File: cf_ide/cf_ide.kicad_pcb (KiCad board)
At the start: 2 copper layers, 17 parts, among them J1 PATA_44pin, J2 Compact_Flash_TrueIDE, U1 74AHC1G02, U2 LT1761-3.3

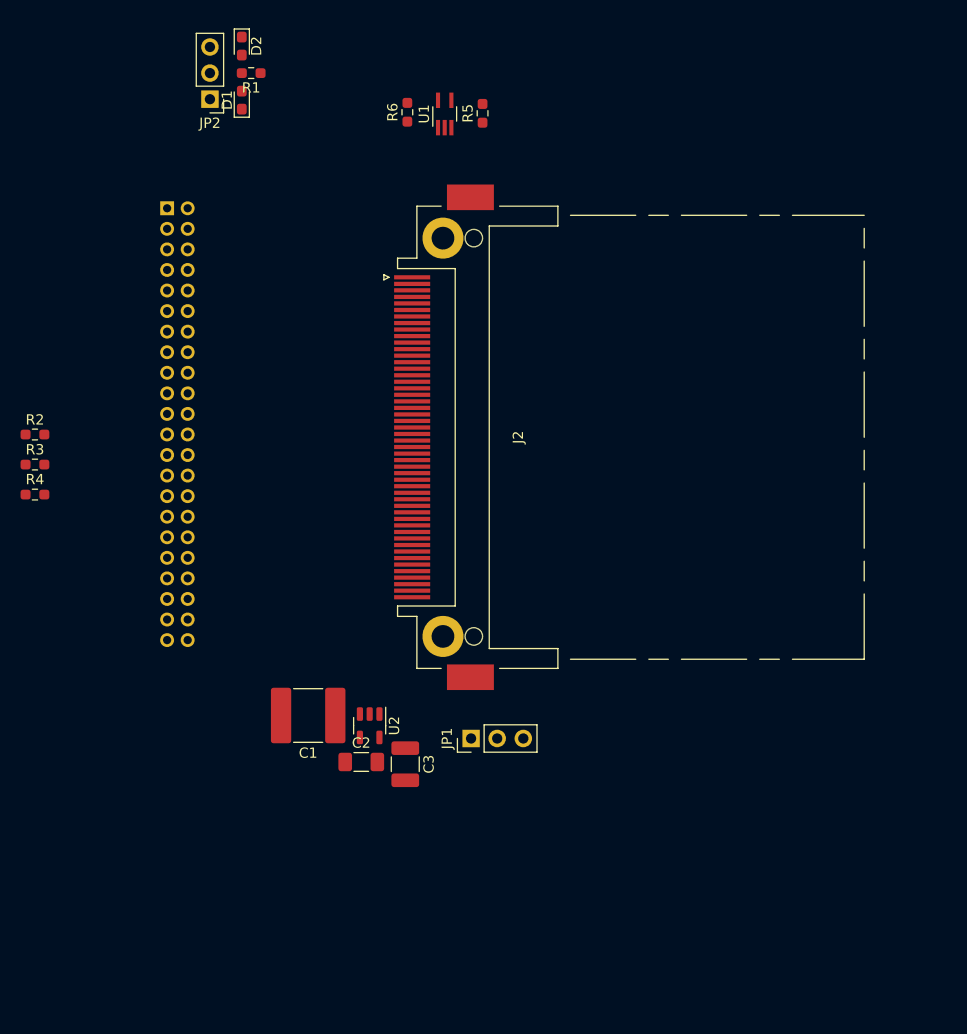
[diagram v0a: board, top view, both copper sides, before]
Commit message: Remove unneeded pull up/downs
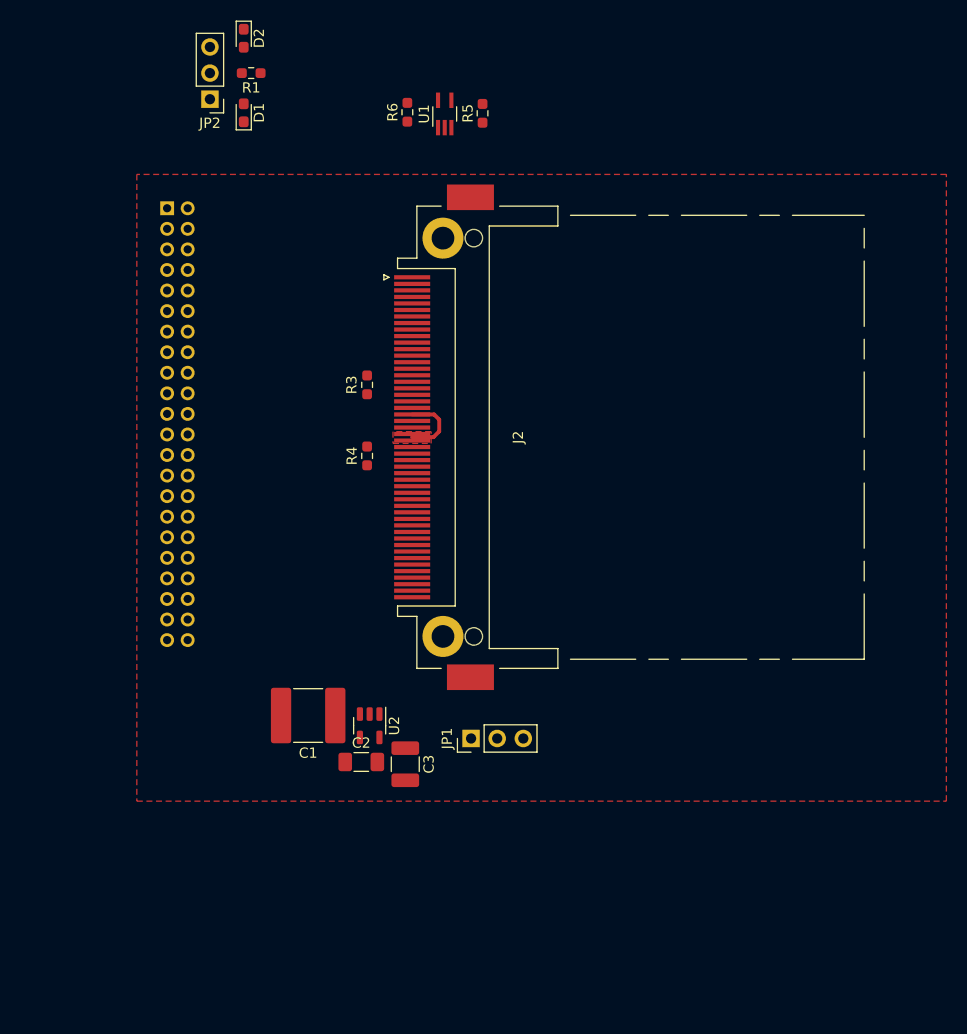
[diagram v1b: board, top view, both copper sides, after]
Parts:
- removed R2: R, Resistor_SMD:R_0603_1608Metric_Pad0.98x0.95mm_HandSolder
- R3, R4: value R -> 47k
- moved R3 33.2 mm to (124.0, 91.6), turned to -90 degrees
- moved R4 32.5 mm to (124.0, 98.5), turned to 90 degrees
- moved D1 1.24 mm to (112.0, 65.1)
- moved D2 0.78 mm to (112.0, 57.9)
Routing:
- net VCC: track 0.00 -> 6.86 mm
- added copper zone on F.Cu, net GNDD
- added copper zone on F.Cu, net VCC

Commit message: Start PCB design
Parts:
- C1: footprint Capacitor_SMD:C_2220_5650Metric_Pad1.97x5.40mm_HandSolder -> Capacitor_SMD:C_0805_2012Metric_Pad1.18x1.45mm_HandSolder; moved to B.Cu
- C2: value 0.1μF -> 0.01μF; moved to B.Cu
- C3, JP1, R3, R4, U2: moved to B.Cu
- moved D1 85.7 mm to (116.8, 150.7)
- moved D2 85.7 mm to (116.8, 143.4)
- moved JP2 85.7 mm to (113.5, 149.4)
- moved R1 85.7 mm to (117.5, 146.8)
- moved R5 75.7 mm to (134.9, 140.8)
- moved R6 75.7 mm to (127.6, 140.7)
- moved U1 75.7 mm to (131.2, 140.9)
- moved C2 64.7 mm to (120.8, 63.7), turned to -90 degrees
- moved C3 61.2 mm to (119.5, 67.8), turned to 180 degrees
- moved U2 60.9 mm to (117.3, 64.2), turned to 0 degrees
- moved C1 56.7 mm to (114.8, 67.2)
- moved JP1 56.1 mm to (124.0, 70.9), turned to 0 degrees
- moved R4 8.59 mm to (132.6, 98.7)
- moved R3 8.59 mm to (132.6, 91.6)
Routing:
- net ~{VS_{2}}: track 0.00 -> 4.23 mm, vias 0 -> 1
- net ~{VS_{1}}: track 0.00 -> 4.23 mm, vias 0 -> 1
- net VCC: track 6.86 -> 8.23 mm
